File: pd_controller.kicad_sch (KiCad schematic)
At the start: 29 parts, among them Q1 IRF9358TRPBF, Q2 BSL308PEH6327XTSA1, Q3 NVTR4503NT1G, U1 CYPD3177-24LQXQT

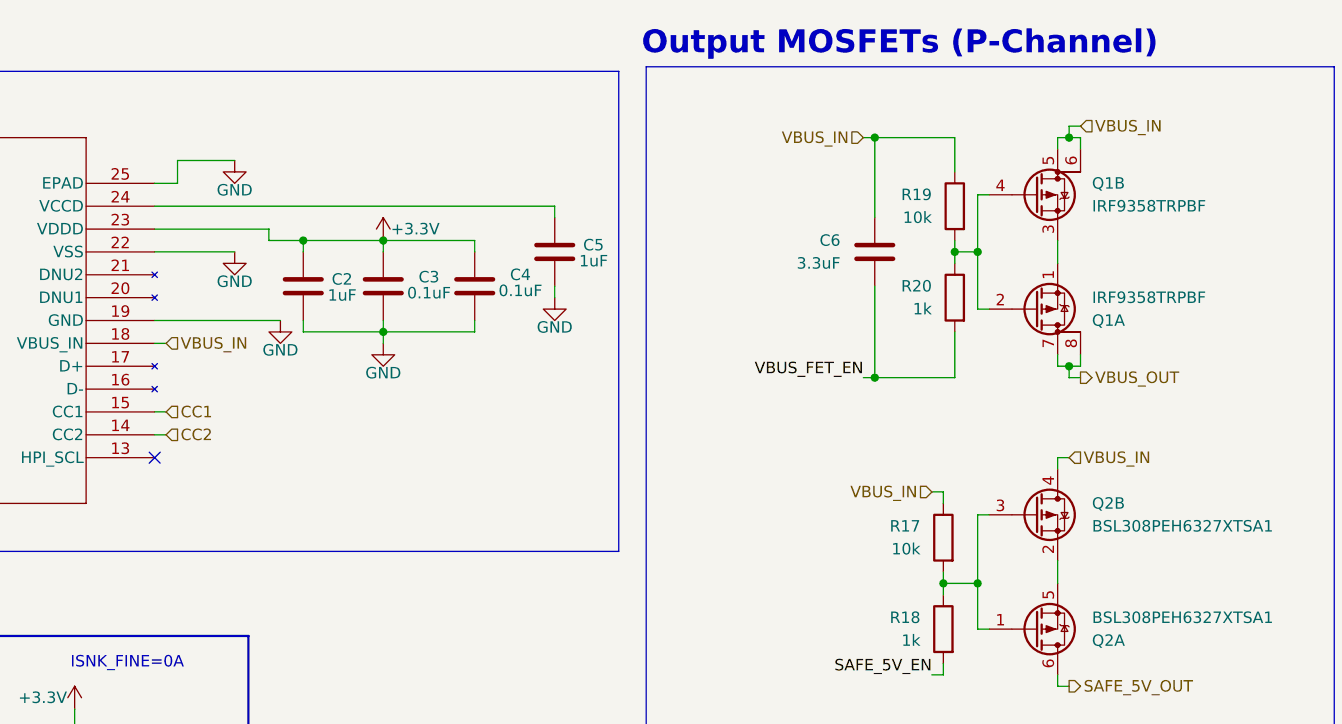
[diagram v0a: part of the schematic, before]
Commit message: changed resistor values on infineon chip output mosfets to match EZ PD BCR datasheet better
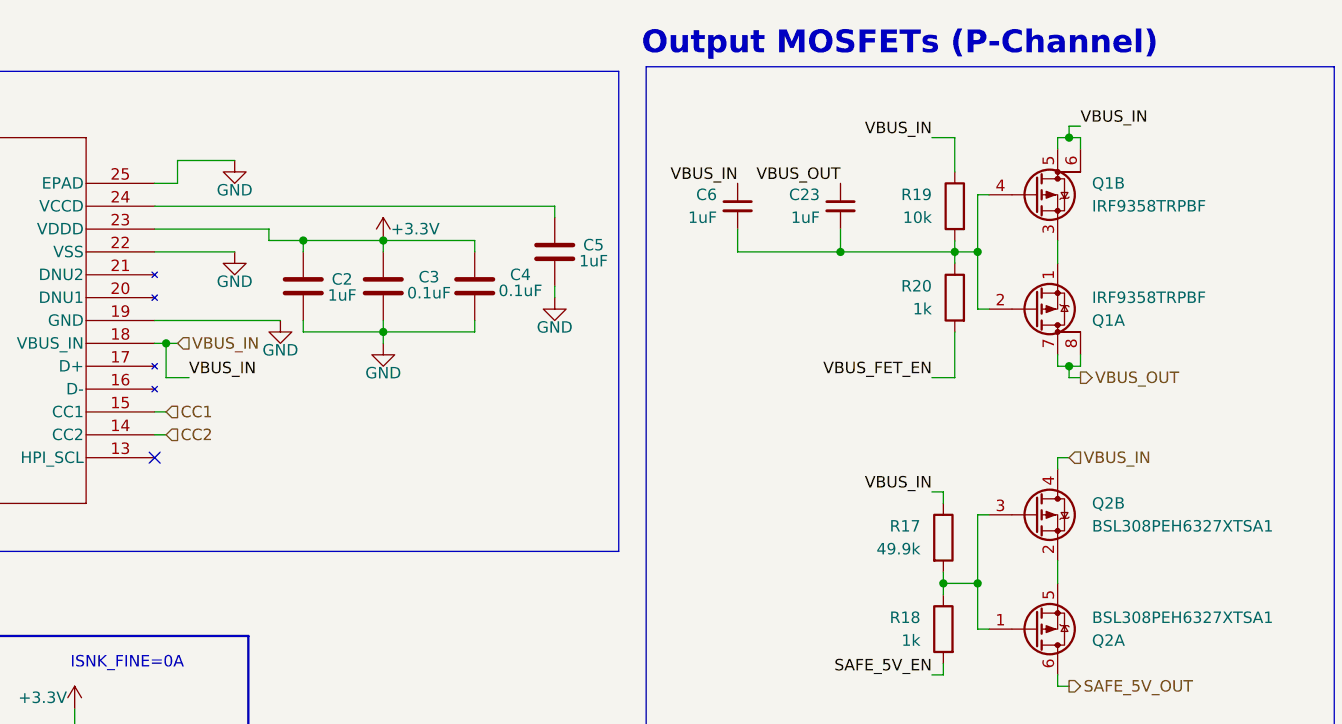
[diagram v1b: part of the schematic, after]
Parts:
- added C23: 1uF, Capacitor_SMD:C_0805_2012Metric, symbol Device:C_Small
- C6: value 3.3uF -> 1uF; symbol Device:C -> Device:C_Small
- R17: value 10k -> 49.9k
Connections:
- net VBUS_FET_EN: no longer C6.2
- net VBUS_OUT: now also C23.1
- net at Q1.2 (G), Q1.4 (G), R19.2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: now also C6.2, C23.2
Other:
- moved on the sheet: C6

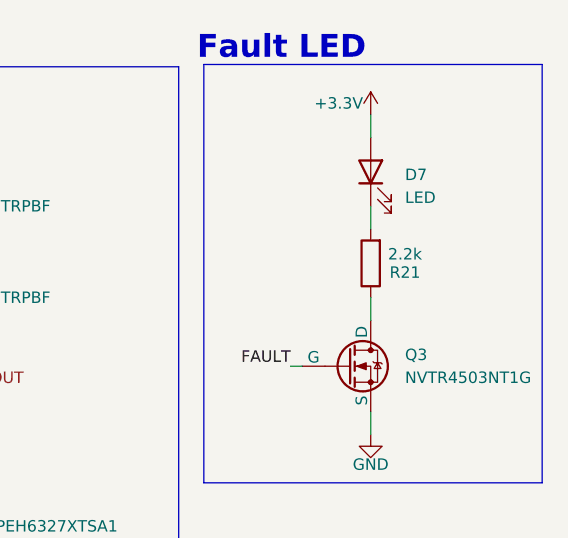
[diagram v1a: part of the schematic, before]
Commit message: address review changes, add more output protections
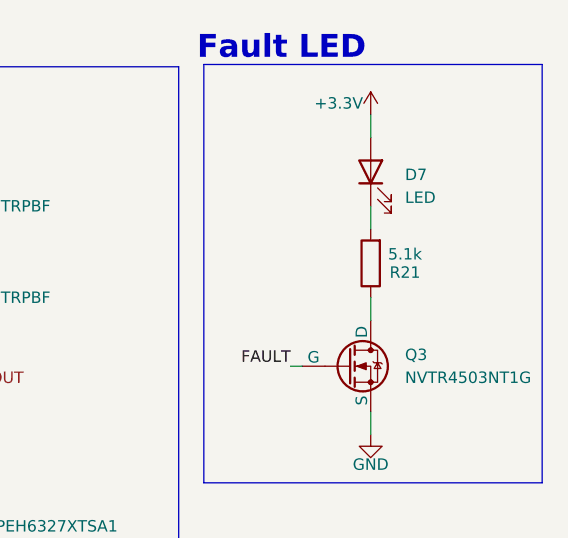
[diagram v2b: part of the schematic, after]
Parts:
- R21: value 2.2k -> 5.1k
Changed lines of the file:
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@@
 			)
 		)
-		(property "Value" "2.2k"
+		(property "Value" "5.1k"
 			(at 267.97 63.754 0)
 			(effects

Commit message: footprint assignment again
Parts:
- renumbered C23 to C7, D7 to D8, TP8 to TP10, TP9 to TP11, TP10 to TP12, TP11 to TP13, U1 to U2
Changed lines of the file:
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@@
 		(on_board yes)
 		(dnp no)
-		(property "Reference" "#PWR022"
+		(property "Reference" "#PWR037"
 			(at 120.65 69.85 0)
 			(effects
@@
 			(project "USBCPowerPCB"
 				(path "/f58400c5-df4b-4929-8d2b-33c0fe23fcd9/4ed27f5f-caef-4817-8da2-6ac4f08dfb73"
-					(reference "#PWR022")
+					(reference "#PWR037")
 					(unit 1)
 				)
@@
 		(dnp no)
 		(fields_autoplaced yes)
-		(property "Reference" "U1"
+		(property "Reference" "U2"
 			(at 81.28 45.72 0)
 			(effects
@@
 			(project "USBCPowerPCB"
 				(path "/f58400c5-df4b-4929-8d2b-33c0fe23fcd9/4ed27f5f-caef-4817-8da2-6ac4f08dfb73"
-					(reference "U1")
+					(reference "U2")
 					(unit 1)
 				)
@@
 		(on_board yes)
 		(dnp no)
-		(property "Reference" "#PWR019"
+		(property "Reference" "#PWR034"
 			(at 102.87 118.11 0)
 			(effects
@@
 			(project "USBCPowerPCB"
 				(path "/f58400c5-df4b-4929-8d2b-33c0fe23fcd9/4ed27f5f-caef-4817-8da2-6ac4f08dfb73"
-					(reference "#PWR019")
+					(reference "#PWR034")
 					(unit 1)
 				)
@@
 		(dnp no)
 		(fields_autoplaced yes)
-		(property "Reference" "#PWR016"
+		(property "Reference" "#PWR031"
 			(at 48.26 143.51 0)
 			(effects
@@
 			(project "USBCPowerPCB"
 				(path "/f58400c5-df4b-4929-8d2b-33c0fe23fcd9/4ed27f5f-caef-4817-8da2-6ac4f08dfb73"
-					(reference "#PWR016")
+					(reference "#PWR031")
 					(unit 1)
 				)
@@
 		(on_board yes)
 		(dnp no)
-		(property "Reference" "#PWR025"
+		(property "Reference" "#PWR040"
 			(at 137.16 80.01 0)
 			(effects
@@
 			(project "USBCPowerPCB"
 				(path "/f58400c5-df4b-4929-8d2b-33c0fe23fcd9/4ed27f5f-caef-4817-8da2-6ac4f08dfb73"
-					(reference "#PWR025")
+					(reference "#PWR040")
 					(unit 1)
 				)
@@
 		(on_board yes)
 		(dnp no)
-		(property "Reference" "#PWR027"
+		(property "Reference" "#PWR042"
 			(at 264.16 52.07 0)
 			(effects
@@
 			(project "USBCPowerPCB"
 				(path "/f58400c5-df4b-4929-8d2b-33c0fe23fcd9/4ed27f5f-caef-4817-8da2-6ac4f08dfb73"
-					(reference "#PWR027")
+					(reference "#PWR042")
 					(unit 1)
 				)
@@
 		(on_board yes)
 		(dnp no)
-		(property "Reference" "#PWR023"
+		(property "Reference" "#PWR038"
 			(at 125.73 77.47 0)
 			(effects
@@
 			(project "USBCPowerPCB"
 				(path "/f58400c5-df4b-4929-8d2b-33c0fe23fcd9/4ed27f5f-caef-4817-8da2-6ac4f08dfb73"
-					(reference "#PWR023")
+					(reference "#PWR038")
 					(unit 1)
 				)
@@
 		(dnp no)
 		(fields_autoplaced yes)
-		(property "Reference" "D7"
+		(property "Reference" "D8"
 			(at 267.97 54.9274 90)
 			(effects
@@
 			(project "USBCPowerPCB"
 				(path "/f58400c5-df4b-4929-8d2b-33c0fe23fcd9/4ed27f5f-caef-4817-8da2-6ac4f08dfb73"
-					(reference "D7")
+					(reference "D8")
 					(unit 1)
 				)
@@
 		(dnp no)
 		(fields_autoplaced yes)
-		(property "Reference" "#PWR018"
+		(property "Reference" "#PWR033"
 			(at 72.39 143.51 0)
 			(effects
@@
 			(project "USBCPowerPCB"
 				(path "/f58400c5-df4b-4929-8d2b-33c0fe23fcd9/4ed27f5f-caef-4817-8da2-6ac4f08dfb73"
-					(reference "#PWR018")
+					(reference "#PWR033")
 					(unit 1)
 				)
@@
 		(on_board yes)
 		(dnp no)
-		(property "Reference" "TP10"
+		(property "Reference" "TP12"
 			(at 90.932 117.602 0)
 			(effects
@@
 			(project "USBCPowerPCB"
 				(path "/f58400c5-df4b-4929-8d2b-33c0fe23fcd9/4ed27f5f-caef-4817-8da2-6ac4f08dfb73"
-					(reference "TP10")
+					(reference "TP12")
 					(unit 1)
 				)
@@
 		(on_board yes)
 		(dnp no)
-		(property "Reference" "TP9"
+		(property "Reference" "TP11"
 			(at 65.532 117.602 0)
 			(effects
@@
 			(project "USBCPowerPCB"
 				(path "/f58400c5-df4b-4929-8d2b-33c0fe23fcd9/4ed27f5f-caef-4817-8da2-6ac4f08dfb73"
-					(reference "TP9")
+					(reference "TP11")
 					(unit 1)
 				)
@@
 		(on_board yes)
 		(dnp no)
-		(property "Reference" "#PWR021"
+		(property "Reference" "#PWR036"
 			(at 120.65 59.69 0)
 			(effects
@@
 			(project "USBCPowerPCB"
 				(path "/f58400c5-df4b-4929-8d2b-33c0fe23fcd9/4ed27f5f-caef-4817-8da2-6ac4f08dfb73"
-					(reference "#PWR021")
+					(reference "#PWR036")
 					(unit 1)
 				)
@@
 		(on_board yes)
 		(dnp no)
-		(property "Reference" "#PWR011"
+		(property "Reference" "#PWR026"
 			(at 27.94 118.11 0)
 			(effects
@@
 			(project "USBCPowerPCB"
 				(path "/f58400c5-df4b-4929-8d2b-33c0fe23fcd9/4ed27f5f-caef-4817-8da2-6ac4f08dfb73"
-					(reference "#PWR011")
+					(reference "#PWR026")
 					(unit 1)
 				)
@@
 		(on_board yes)
 		(dnp no)
-		(property "Reference" "TP11"
+		(property "Reference" "TP13"
 			(at 116.332 117.602 0)
 			(effects
@@
 			(project "USBCPowerPCB"
 				(path "/f58400c5-df4b-4929-8d2b-33c0fe23fcd9/4ed27f5f-caef-4817-8da2-6ac4f08dfb73"
-					(reference "TP11")
+					(reference "TP13")
 					(unit 1)
 				)
@@
 		(on_board yes)
 		(dnp no)
-		(property "Reference" "C23"
+		(property "Reference" "C7"
 			(at 185.674 57.15 0)
 			(effects
@@
 			(project "USBCPowerPCB"
 				(path "/f58400c5-df4b-4929-8d2b-33c0fe23fcd9/4ed27f5f-caef-4817-8da2-6ac4f08dfb73"
-					(reference "C23")
+					(reference "C7")
 					(unit 1)
 				)
@@
 		(on_board yes)
 		(dnp no)
-		(property "Reference" "#PWR026"
+		(property "Reference" "#PWR041"
 			(at 156.21 74.93 0)
 			(effects
@@
 			(project "USBCPowerPCB"
 				(path "/f58400c5-df4b-4929-8d2b-33c0fe23fcd9/4ed27f5f-caef-4817-8da2-6ac4f08dfb73"
-					(reference "#PWR026")
+					(reference "#PWR041")
 					(unit 1)
 				)
@@
 		(on_board yes)
 		(dnp no)
-		(property "Reference" "#PWR015"
+		(property "Reference" "#PWR030"
 			(at 48.26 118.11 0)
 			(effects
@@
 			(project "USBCPowerPCB"
 				(path "/f58400c5-df4b-4929-8d2b-33c0fe23fcd9/4ed27f5f-caef-4817-8da2-6ac4f08dfb73"
-					(reference "#PWR015")
+					(reference "#PWR030")
 					(unit 1)
 				)
@@
 		(on_board yes)
 		(dnp no)
-		(property "Reference" "#PWR024"
+		(property "Reference" "#PWR039"
 			(at 137.16 66.04 0)
 			(effects
@@
 			(project "USBCPowerPCB"
 				(path "/f58400c5-df4b-4929-8d2b-33c0fe23fcd9/4ed27f5f-caef-4817-8da2-6ac4f08dfb73"
-					(reference "#PWR024")
+					(reference "#PWR039")
 					(unit 1)
 				)
@@
 		(on_board yes)
 		(dnp no)
-		(property "Reference" "#PWR014"
+		(property "Reference" "#PWR029"
 			(at 38.1 97.79 0)
 			(effects
@@
 			(project "USBCPowerPCB"
 				(path "/f58400c5-df4b-4929-8d2b-33c0fe23fcd9/4ed27f5f-caef-4817-8da2-6ac4f08dfb73"
-					(reference "#PWR014")
+					(reference "#PWR029")
 					(unit 1)
 				)
@@
 		(dnp no)
 		(fields_autoplaced yes)
-		(property "Reference" "#PWR020"
+		(property "Reference" "#PWR035"
 			(at 102.87 143.51 0)
 			(effects
@@
 			(project "USBCPowerPCB"
 				(path "/f58400c5-df4b-4929-8d2b-33c0fe23fcd9/4ed27f5f-caef-4817-8da2-6ac4f08dfb73"
-					(reference "#PWR020")
+					(reference "#PWR035")
 					(unit 1)
 				)
@@
 		(dnp no)
 		(fields_autoplaced yes)
-		(property "Reference" "#PWR012"
+		(property "Reference" "#PWR027"
 			(at 27.94 143.51 0)
 			(effects
@@
 			(project "USBCPowerPCB"
 				(path "/f58400c5-df4b-4929-8d2b-33c0fe23fcd9/4ed27f5f-caef-4817-8da2-6ac4f08dfb73"
-					(reference "#PWR012")
+					(reference "#PWR027")
 					(unit 1)
 				)
@@
 		(on_board yes)
 		(dnp no)
-		(property "Reference" "TP8"
+		(property "Reference" "TP10"
 			(at 45.212 117.602 0)
 			(effects
@@
 			(project "USBCPowerPCB"
 				(path "/f58400c5-df4b-4929-8d2b-33c0fe23fcd9/4ed27f5f-caef-4817-8da2-6ac4f08dfb73"
-					(reference "TP8")
+					(reference "TP10")
 					(unit 1)
 				)
@@
 		(on_board yes)
 		(dnp no)
-		(property "Reference" "#PWR013"
+		(property "Reference" "#PWR028"
 			(at 35.56 72.39 0)
 			(effects
@@
 			(project "USBCPowerPCB"
 				(path "/f58400c5-df4b-4929-8d2b-33c0fe23fcd9/4ed27f5f-caef-4817-8da2-6ac4f08dfb73"
-					(reference "#PWR013")
+					(reference "#PWR028")
 					(unit 1)
 				)
@@
 		(on_board yes)
 		(dnp no)
-		(property "Reference" "#PWR017"
+		(property "Reference" "#PWR032"
 			(at 72.39 118.11 0)
 			(effects
@@
 			(project "USBCPowerPCB"
 				(path "/f58400c5-df4b-4929-8d2b-33c0fe23fcd9/4ed27f5f-caef-4817-8da2-6ac4f08dfb73"
-					(reference "#PWR017")
+					(reference "#PWR032")
 					(unit 1)
 				)
@@
 		(on_board yes)
 		(dnp no)
-		(property "Reference" "#PWR028"
+		(property "Reference" "#PWR043"
 			(at 264.16 90.17 0)
 			(effects
@@
 			(project "USBCPowerPCB"
 				(path "/f58400c5-df4b-4929-8d2b-33c0fe23fcd9/4ed27f5f-caef-4817-8da2-6ac4f08dfb73"
-					(reference "#PWR028")
+					(reference "#PWR043")
 					(unit 1)
 				)

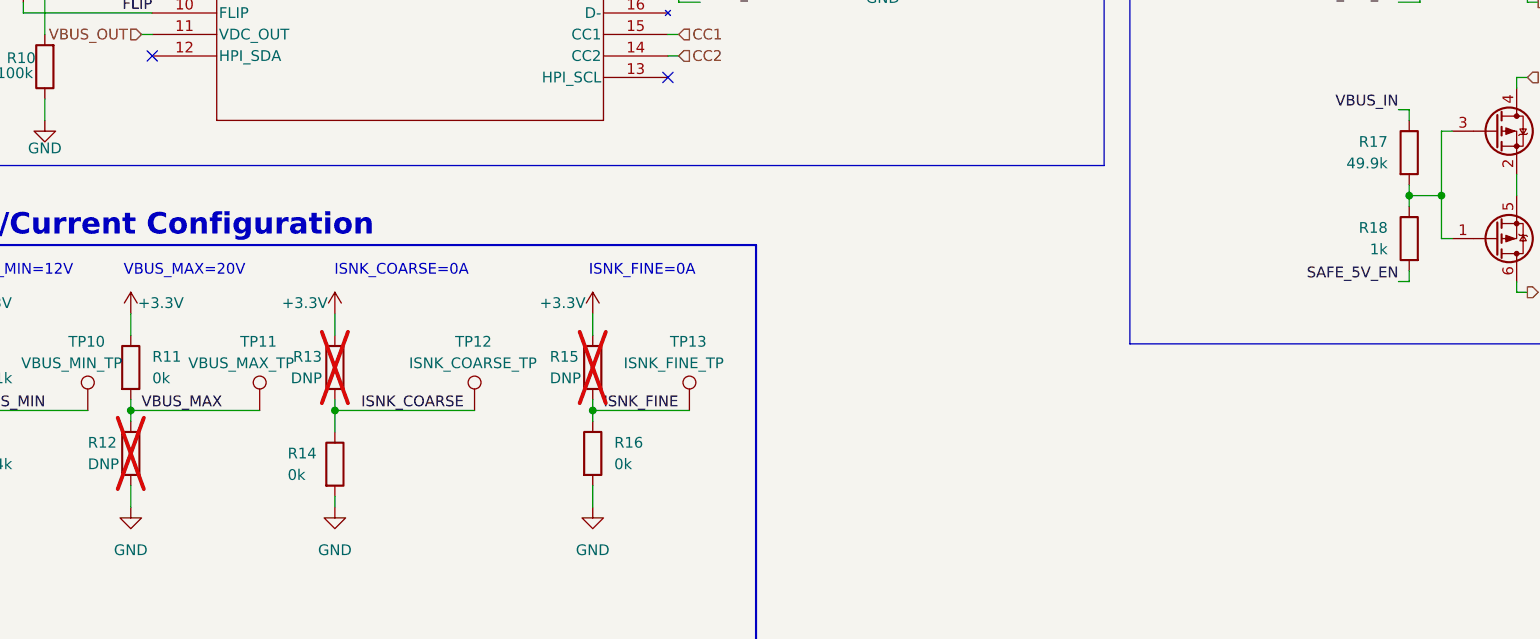
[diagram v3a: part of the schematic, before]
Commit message: finished addressing review comments & organized bom with p/ns for everything
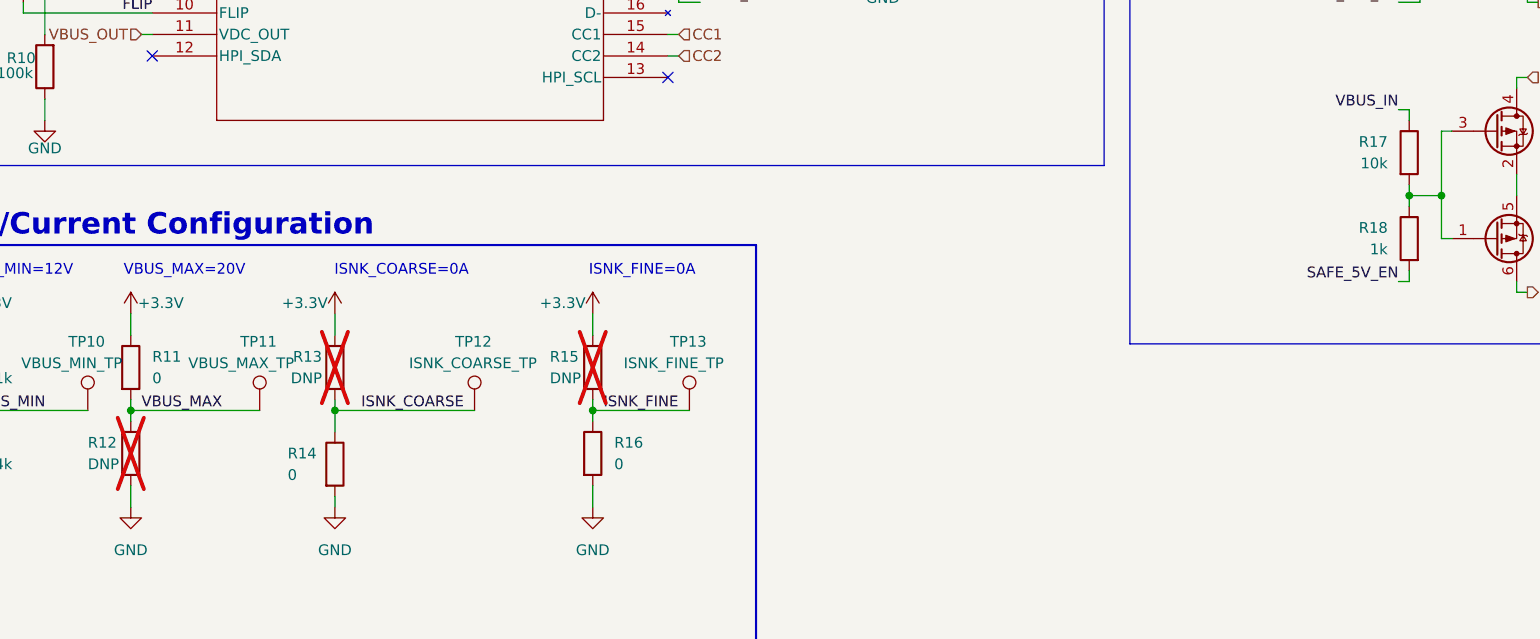
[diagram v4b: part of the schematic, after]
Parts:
- C2, C5, C6, C7: Manufacturer_Name (none) -> KEMET; Mouser Part Number (none) -> C0805C105K5PACTU; Vdc (none) -> 50V
- C3, C4: Manufacturer_Name (none) -> KEMET; Mouser Part Number (none) -> C0805C104M5RACTU; Vdc (none) -> 50V
- D8: Manufacturer_Name (none) -> Kingbright; Mouser Part Number APTD2012LCGCK -> 604-APTD2012LCGCK
- R10: Manufacturer_Name (none) -> VISHAY; Mouser Part Number (none) -> CRCW0805100KFKEAC
- R11, R14, R16: value 0k -> 0
- R17: value 49.9k -> 10k; Manufacturer_Name (none) -> VISHAY; Mouser Part Number (none) -> CRCW080510K0FKEAC
- R18, R20: Manufacturer_Name (none) -> VISHAY; Mouser Part Number (none) -> CRCW08051K00FKEAC
- R19: Manufacturer_Name (none) -> VISHAY; Mouser Part Number (none) -> CRCW080510K0FKEAC
- R21, R7: Manufacturer_Name (none) -> VISHAY; Mouser Part Number (none) -> CRCW08055K10FKEAC
- R8: Manufacturer_Name (none) -> VISHAY; Mouser Part Number (none) -> CRCW08052K40FKEAC
- R9: Manufacturer_Name (none) -> VISHAY; Mouser Part Number (none) -> CRCW08054K70FKEAC
- U2: Manufacturer_Name (none) -> Infineon; Mouser Part Number (none) -> 727-CYPD3177-24LQXQT
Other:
- title: (none) -> Power Delivery Controller

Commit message: intermediate progress push before addressing Champers' and Lakshay's review comments
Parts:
- removed Q3: NVTR4503NT1G, Package_TO_SOT_SMD:SOT-23-3, symbol Simulation_SPICE:NMOS
- renumbered C2 to C3, C3 to C4, C4 to C5, C5 to C6, C6 to C7, C7 to C8
